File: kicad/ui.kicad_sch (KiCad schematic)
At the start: 52 parts, among them J7 Conn_02x05_Odd_Even, SW1 RotaryEncoder_Switch, SW2 RotaryEncoder_Switch, SW302 SW_Push_45deg, U11 M24C32-RMN, U16 74AC14, U3 Pico, U301 74AC14, U9 SN75176BP

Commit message: Compile gerber and drill files in one zip
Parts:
- added SW301, SW303, SW304, SW305: SW_Push_45deg, symbol Switch:SW_Push_45deg
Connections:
- net GND: now also SW302.2, SW301.2, SW303.2, SW304.2, SW305.2
- net SWin7: now reaches SW302.1
- new net SWin10: SW304.1
- new net SWin11: SW305.1
- new net SWin8: SW301.1
- new net SWin9: SW303.1
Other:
- moved on the sheet: SW302
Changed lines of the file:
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@@
   (junction (at -16.51 85.09) (diameter 0) (color 0 0 0 0)
   )
+  (junction (at 129.54 116.84) (diameter 0) (color 0 0 0 0)
+  )
   (junction (at 59.69 27.94) (diameter 0) (color 0 0 0 0)
   )
@@
   (junction (at 280.67 43.18) (diameter 0) (color 0 0 0 0)
   )
+  (junction (at 132.08 116.84) (diameter 0) (color 0 0 0 0)
+  )
   (junction (at -16.51 82.55) (diameter 0) (color 0 0 0 0)
   )
@@
   )
   (junction (at -40.64 80.01) (diameter 0) (color 0 0 0 0)
+  )
+  (junction (at 142.24 116.84) (diameter 0) (color 0 0 0 0)
   )
   (no_connect (at -19.05 175.26))
@@
     (stroke (width 0) (type default))
   )
+  (wire (pts (xy 129.54 116.84) (xy 132.08 116.84))
+    (stroke (width 0) (type default))
+  )
   (wire (pts (xy 177.8 29.21) (xy 177.8 27.94))
     (stroke (width 0) (type default))
@@
     (stroke (width 0) (type default))
   )
+  (wire (pts (xy 132.08 116.84) (xy 132.08 104.14))
+    (stroke (width 0) (type default))
+  )
   (wire (pts (xy -6.35 180.34) (xy 0 180.34))
     (stroke (width 0) (type default))
@@
     (stroke (width 0) (type default))
   )
+  (wire (pts (xy 132.08 116.84) (xy 142.24 116.84))
+    (stroke (width 0) (type default))
+  )
   (wire (pts (xy 138.43 39.37) (xy 138.43 36.83))
     (stroke (width 0) (type default))
@@
     (stroke (width 0) (type default))
   )
+  (wire (pts (xy 132.08 129.54) (xy 132.08 116.84))
+    (stroke (width 0) (type default))
+  )
   (wire (pts (xy 226.06 125.73) (xy 226.06 133.35))
     (stroke (width 0) (type default))
@@
     (stroke (width 0) (type default))
   )
+  (wire (pts (xy 142.24 116.84) (xy 142.24 119.38))
+    (stroke (width 0) (type default))
+  )
   (bus (pts (xy 2.54 175.26) (xy 2.54 180.34))
     (stroke (width 0) (type default))
   )
+  (wire (pts (xy 129.54 104.14) (xy 132.08 104.14))
+    (stroke (width 0) (type default))
+  )
   (wire (pts (xy 138.43 55.88) (xy 144.78 55.88))
     (stroke (width 0) (type default))
@@
     (stroke (width 0) (type default))
   )
+  (wire (pts (xy 116.84 116.84) (xy 129.54 116.84))
+    (stroke (width 0) (type default))
+  )
   (wire (pts (xy 99.06 55.88) (xy 97.79 55.88))
     (stroke (width 0) (type default))
@@
     (stroke (width 0) (type default))
   )
+  (wire (pts (xy 129.54 129.54) (xy 132.08 129.54))
+    (stroke (width 0) (type default))
+  )
   (wire (pts (xy 128.27 26.67) (xy 128.27 27.94))
     (stroke (width 0) (type default))
@@
     (effects (font (size 1.27 1.27)) (justify right bottom))
   )
+  (label "SWin9" (at 124.46 111.76 180) (fields_autoplaced)
+    (effects (font (size 1.27 1.27)) (justify right bottom))
+  )
   (label "SCL" (at -20.32 177.8 180) (fields_autoplaced)
     (effects (font (size 1.27 1.27)) (justify right bottom))
@@
     (effects (font (size 1.27 1.27)) (justify left bottom))
   )
+  (label "SWin7" (at 124.46 99.06 180) (fields_autoplaced)
+    (effects (font (size 1.27 1.27)) (justify right bottom))
+  )
   (label "SWin4" (at 167.64 27.94 180) (fields_autoplaced)
     (effects (font (size 1.27 1.27)) (justify right bottom))
@@
     (effects (font (size 1.27 1.27)) (justify left bottom))
   )
+  (label "SWin10" (at 137.16 111.76 180) (fields_autoplaced)
+    (effects (font (size 1.27 1.27)) (justify right bottom))
+  )
   (label "GND" (at 177.8 39.37 0) (fields_autoplaced)
     (effects (font (size 1.27 1.27)) (justify left bottom))
@@
     (effects (font (size 1.27 1.27)) (justify right bottom))
   )
+  (label "SWin8" (at 111.76 111.76 180) (fields_autoplaced)
+    (effects (font (size 1.27 1.27)) (justify right bottom))
+  )
   (label "GND" (at 99.06 67.31 0) (fields_autoplaced)
     (effects (font (size 1.27 1.27)) (justify left bottom))
@@
     (effects (font (size 1.27 1.27)) (justify right bottom))
   )
+  (label "SWin11" (at 124.46 124.46 180) (fields_autoplaced)
+    (effects (font (size 1.27 1.27)) (justify right bottom))
+  )
   (label "GND" (at 59.69 39.37 0) (fields_autoplaced)
     (effects (font (size 1.27 1.27)) (justify left bottom))
@@
   (label "GND" (at 45.72 102.87 270) (fields_autoplaced)
     (effects (font (size 1.27 1.27)) (justify right bottom))
+  )
+  (label "GND" (at 142.24 119.38 0) (fields_autoplaced)
+    (effects (font (size 1.27 1.27)) (justify left bottom))
   )
   (label "SWout1" (at 78.74 146.05 90) (fields_autoplaced)
@@
     )
   )
+  (symbol (lib_id "Switch:SW_Push_45deg") (at 114.3 114.3 0) (unit 1)
+    (in_bom yes) (on_board yes) (dnp no) (fields_autoplaced)
+    (property "Reference" "SW301" (at 114.3 106.68 0)
+      (effects (font (size 1.27 1.27)))
+    )
+    (property "Value" "SW_Push_45deg" (at 114.3 109.22 0)
+      (effects (font (size 1.27 1.27)))
+    )
+    (property "Footprint" "" (at 114.3 114.3 0)
+      (effects (font (size 1.27 1.27)) hide)
+    )
+    (property "Datasheet" "~" (at 114.3 114.3 0)
+      (effects (font (size 1.27 1.27)) hide)
+    )
+    (pin "1")
+    (pin "2")
+    (instances
+      (project "digipsu"
+        (path "/ec5fec7a-fde3-4f44-b689-61159deeeb72/4943d487-6290-480b-b97a-e25fc46bcb0d"
+          (reference "SW301") (unit 1)
+        )
+      )
+    )
+  )
   (symbol (lib_id "PCM_kikit:Board") (at 260.35 157.48 0) (unit 1)
     (in_bom no) (on_board yes) (dnp no) (fields_autoplaced)
@@
         (path "/ec5fec7a-fde3-4f44-b689-61159deeeb72/4943d487-6290-480b-b97a-e25fc46bcb0d"
           (reference "R305") (unit 1)
+        )
+      )
+    )
+  )
+  (symbol (lib_id "Switch:SW_Push_45deg") (at 139.7 114.3 0) (unit 1)
+    (in_bom yes) (on_board yes) (dnp no) (fields_autoplaced)
+    (property "Reference" "SW304" (at 139.7 106.68 0)
+      (effects (font (size 1.27 1.27)))
+    )
+    (property "Value" "SW_Push_45deg" (at 139.7 109.22 0)
+      (effects (font (size 1.27 1.27)))
+    )
+    (property "Footprint" "" (at 139.7 114.3 0)
+      (effects (font (size 1.27 1.27)) hide)
+    )
+    (property "Datasheet" "~" (at 139.7 114.3 0)
+      (effects (font (size 1.27 1.27)) hide)
+    )
+    (pin "1")
+    (pin "2")
+    (instances
+      (project "digipsu"
+        (path "/ec5fec7a-fde3-4f44-b689-61159deeeb72/4943d487-6290-480b-b97a-e25fc46bcb0d"
+          (reference "SW304") (unit 1)
         )
       )
@@
     )
   )
+  (symbol (lib_id "Switch:SW_Push_45deg") (at 127 127 0) (unit 1)
+    (in_bom yes) (on_board yes) (dnp no)
+    (property "Reference" "SW305" (at 127 119.38 0)
+      (effects (font (size 1.27 1.27)))
+    )
+    (property "Value" "SW_Push_45deg" (at 127 121.92 0)
+      (effects (font (size 1.27 1.27)))
+    )
+    (property "Footprint" "" (at 127 127 0)
+      (effects (font (size 1.27 1.27)) hide)
+    )
+    (property "Datasheet" "~" (at 127 127 0)
+      (effects (font (size 1.27 1.27)) hide)
+    )
+    (pin "1")
+    (pin "2")
+    (instances
+      (project "digipsu"
+        (path "/ec5fec7a-fde3-4f44-b689-61159deeeb72/4943d487-6290-480b-b97a-e25fc46bcb0d"
+          (reference "SW305") (unit 1)
+        )
+      )
+    )
+  )
   (symbol (lib_id "Device:R") (at 133.35 55.88 270) (mirror x) (unit 1)
     (in_bom yes) (on_board yes) (dnp no)
@@
     )
   )
-  (symbol (lib_id "Switch:SW_Push_45deg") (at 46.99 125.73 0) (unit 1)
-    (in_bom yes) (on_board yes) (dnp no) (fields_autoplaced)
-    (property "Reference" "SW302" (at 46.99 118.11 0)
-      (effects (font (size 1.27 1.27)))
-    )
-    (property "Value" "SW_Push_45deg" (at 46.99 120.65 0)
-      (effects (font (size 1.27 1.27)))
-    )
-    (property "Footprint" "" (at 46.99 125.73 0)
-      (effects (font (size 1.27 1.27)) hide)
-    )
-    (property "Datasheet" "~" (at 46.99 125.73 0)
+  (symbol (lib_id "Switch:SW_Push_45deg") (at 127 101.6 0) (unit 1)
+    (in_bom yes) (on_board yes) (dnp no) (fields_autoplaced)
+    (property "Reference" "SW302" (at 127 93.98 0)
+      (effects (font (size 1.27 1.27)))
+    )
+    (property "Value" "SW_Push_45deg" (at 127 96.52 0)
+      (effects (font (size 1.27 1.27)))
+    )
+    (property "Footprint" "" (at 127 101.6 0)
+      (effects (font (size 1.27 1.27)) hide)
+    )
+    (property "Datasheet" "~" (at 127 101.6 0)
       (effects (font (size 1.27 1.27)) hide)
     )
@@
         )
       )
+    )
+  )
+  (symbol (lib_id "Switch:SW_Push_45deg") (at 127 114.3 0) (unit 1)
+    (in_bom yes) (on_board yes) (dnp no) (fields_autoplaced)
+    (property "Reference" "SW303" (at 127 106.68 0)
+      (effects (font (size 1.27 1.27)))
+    )
+    (property "Value" "SW_Push_45deg" (at 127 109.22 0)
+      (effects (font (size 1.27 1.27)))
+    )
+    (property "Footprint" "" (at 127 114.3 0)
+      (effects (font (size 1.27 1.27)) hide)
+    )
+    (property "Datasheet" "~" (at 127 114.3 0)
+      (effects (font (size 1.27 1.27)) hide)
+    )
+    (pin "1")
+    (pin "2")
+    (instances
+      (project "digipsu"
+        (path "/ec5fec7a-fde3-4f44-b689-61159deeeb72/4943d487-6290-480b-b97a-e25fc46bcb0d"
+          (reference "SW303") (unit 1)
+        )
+      )

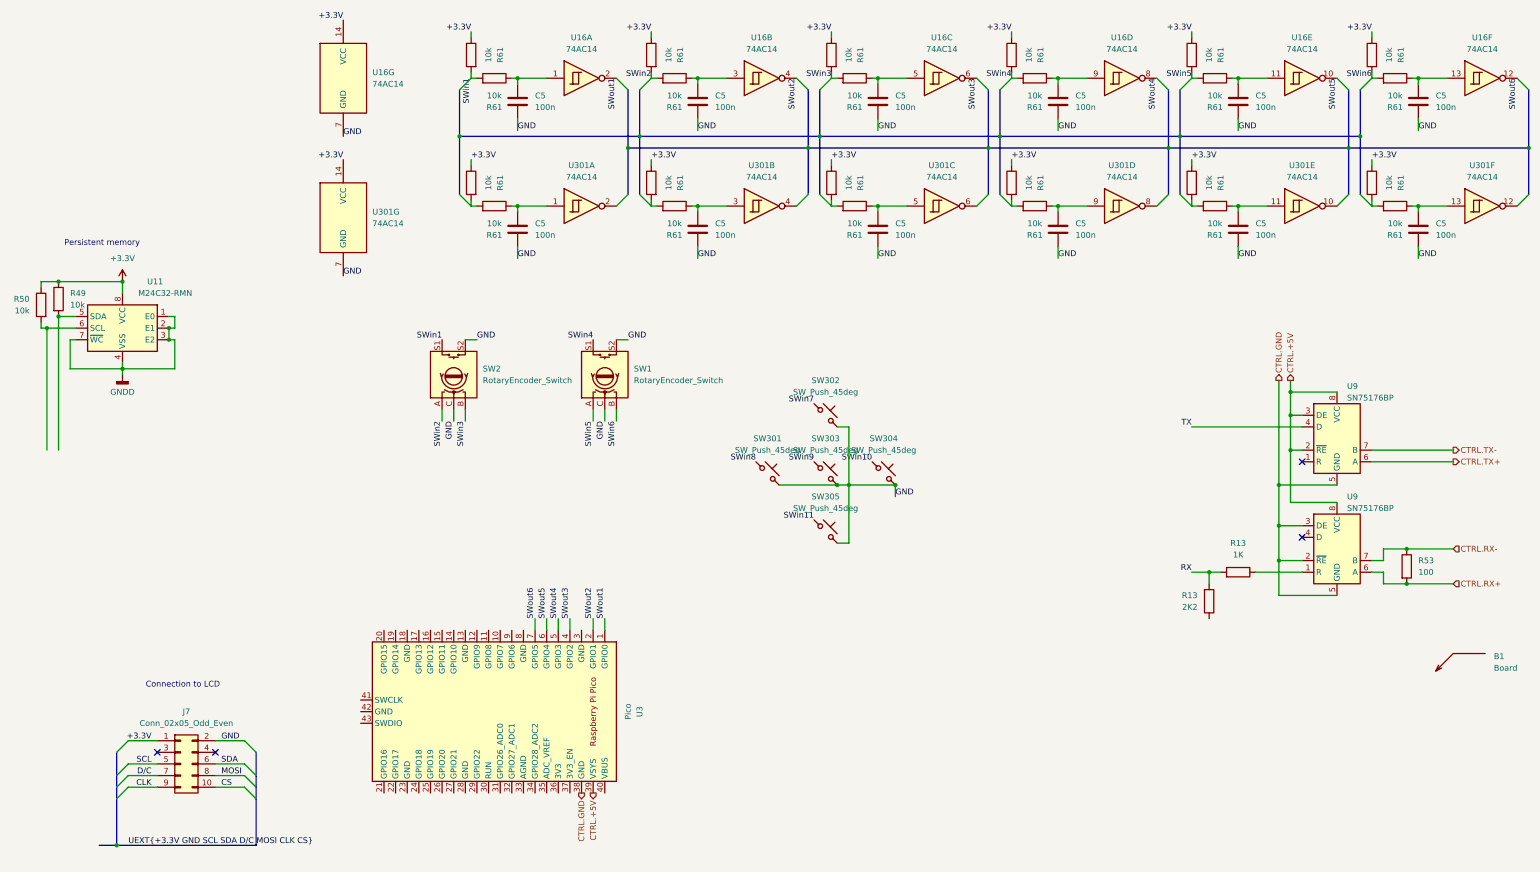
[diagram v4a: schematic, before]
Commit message: Start UI pcb design
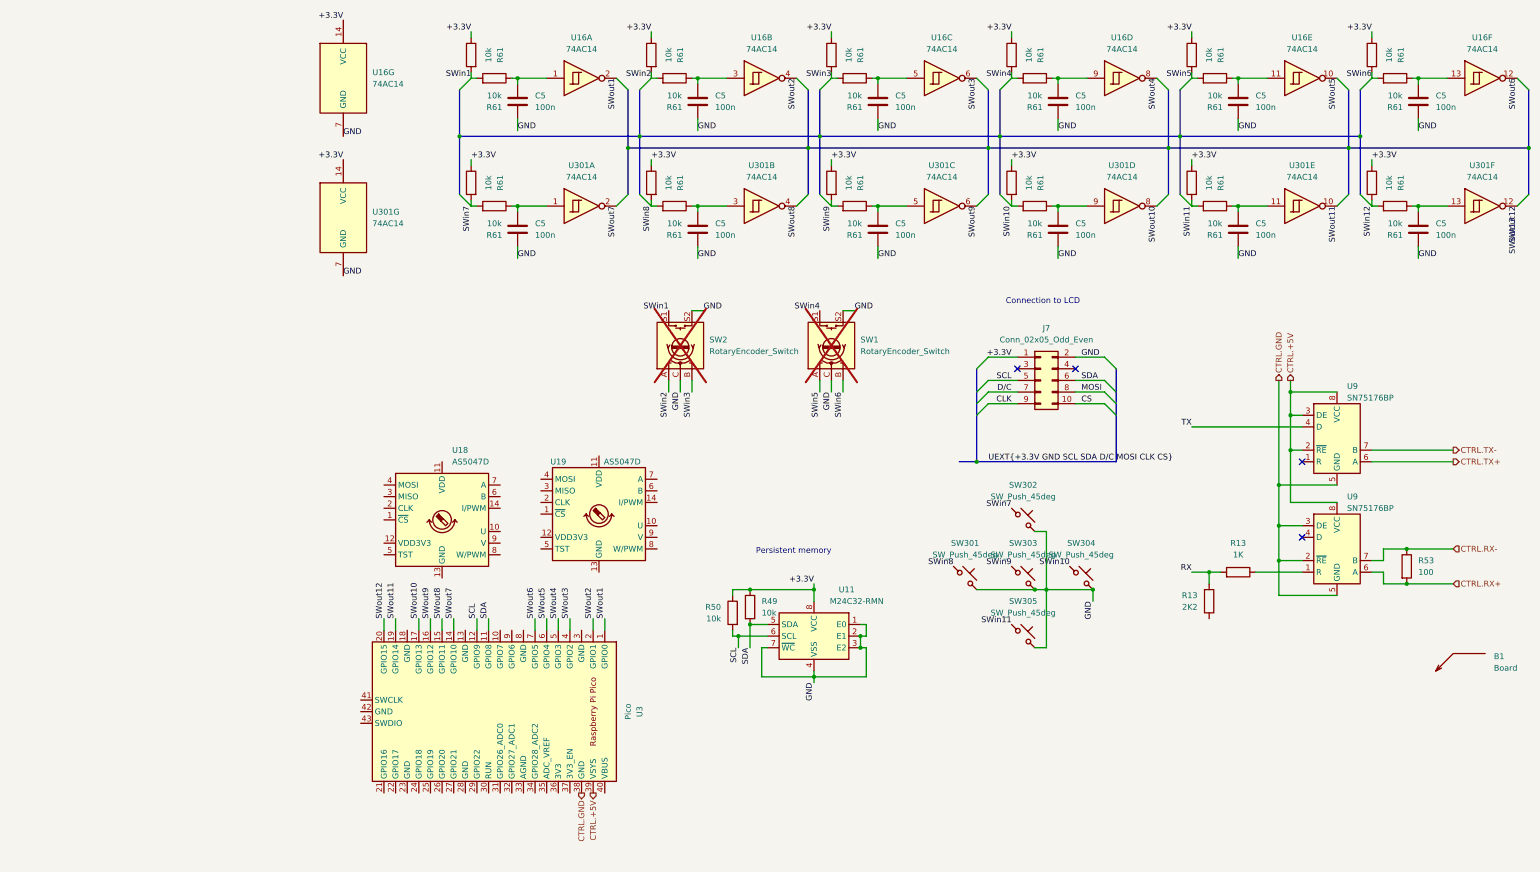
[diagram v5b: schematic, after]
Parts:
- added U18, U19: AS5047D, Package_SO:TSSOP-14_4.4x5mm_P0.65mm, symbol Sensor_Magnetic:AS5047D
- J7: footprint (none) -> Connector_IDC:IDC-Header_2x05_P2.54mm_Vertical
- SW1, SW2: now not fitted
- SW301, SW302, SW303, SW304, SW305: footprint (none) -> Button_Switch_THT:SW_PUSH_6mm
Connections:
- net GNDD is gone; now on net GND: U11.1 (E0), U11.2 (E1), U11.3 (E2), U11.4 (VSS), U11.7 (~{WC})
- net SCL: now also R50.2, U11.6 (SCL), U3.12 (GPIO9)
- net SDA: now also R49.2, U11.5 (SDA), U3.11 (GPIO8)
- net SWin10: now also R61.2, R61.2
- net SWin11: now also R61.2, R61.2
- net SWin7: now also R61.2, R61.2
- net SWin8: now also R61.2, R61.2
- net SWin9: now also R61.2, R61.2
- net SWout7: now reaches U3.14 (GPIO10)
- net SWout7: now also U301.2
- net SWout8: now reaches U3.15 (GPIO11)
- net SWout8: now also U301.4
- net SWout9: now reaches U3.16 (GPIO12)
- net SWout9: now also U301.6
- net SWout10: now reaches U3.17 (GPIO13)
- net SWout10: now also U301.8
- net SWout11: now reaches U3.19 (GPIO14)
- net SWout11: now also U301.10
- net SWout12: now reaches U3.20 (GPIO15)
- net SWout12: now also U301.12
- net SWin12: now reaches R61.2, R61.2
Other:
- moved on the sheet: J7, R49, R50, SW301, SW302, SW303, SW304, SW305, U11

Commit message: Continue on UI board design
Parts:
- added C5 (x2): 100n, Capacitor_THT:C_Disc_D3.8mm_W2.6mm_P2.50mm, symbol Device:C
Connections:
- net GND is gone; now on net CTRL.GND: C5.2, C5.2, C5.2, C5.2, C5.2, C5.2, C5.2, C5.2, C5.2, C5.2, C5.2, C5.2, J7.2 (Pin_2), SW1.C, SW1.S2, SW2.C, SW2.S2, SW301.2, SW302.2, SW303.2, SW304.2, SW305.2, U11.1 (E0), U11.2 (E1), U11.3 (E2), U11.4 (VSS), U11.7 (~{WC}), U16.7 (GND), U301.7 (GND)
- net +3.3V: now also U3.36 (3V3)
- net CTRL.GND: now also R13.1, U18.13 (GND), U18.5 (TST), U19.13 (GND), U19.5 (TST), C5.2, C5.2
- net RX: now also U3.2 (GPIO1)
- net SWout1: now also U3.4 (GPIO2); no longer U3.1 (GPIO0)
- net SWout10: now also U3.24 (GPIO18); no longer U3.17 (GPIO13)
- net SWout11: now also U3.22 (GPIO17); no longer U3.19 (GPIO14)
- net SWout12: now also U3.21 (GPIO16); no longer U3.20 (GPIO15)
- net SWout2: now also U18.6 (B), U18.7 (A), U3.5 (GPIO3); no longer U3.2 (GPIO1)
- net SWout3: now also U3.6 (GPIO4); no longer U3.4 (GPIO2)
- net SWout4: now also U3.7 (GPIO5); no longer U3.5 (GPIO3)
- net SWout5: now also U19.7 (A), U3.9 (GPIO6); no longer U3.6 (GPIO4)
- net SWout6: now also U19.6 (B), U3.10 (GPIO7); no longer U3.7 (GPIO5)
- net SWout7: now also U3.27 (GPIO21); no longer U3.14 (GPIO10)
- net SWout8: now also U3.26 (GPIO20); no longer U3.15 (GPIO11)
- net SWout9: now also U3.25 (GPIO19); no longer U3.16 (GPIO12)
- net TX: now also U3.1 (GPIO0)
- net ENC.CS1: now reaches U18.1 (~{CS})
- net at U18.11 (VDD): now also U18.12 (VDD3V3), C5.1
- net ENC.CLK: now reaches U18.2 (CLK)
- net ENC.CLK: now also U19.2 (CLK)
- net ENC.MISO: now reaches U18.3 (MISO)
- net ENC.MISO: now also U19.3 (MISO)
- net ENC.MOSI: now reaches U18.4 (MOSI)
- net ENC.MOSI: now also U19.4 (MOSI)
- net ENC.CS2: now reaches U19.1 (~{CS})
- net at U19.11 (VDD): now also U19.12 (VDD3V3), C5.1
- no-connect marks 4 -> 12
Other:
- moved on the sheet: SW1, SW2, U18, U19
